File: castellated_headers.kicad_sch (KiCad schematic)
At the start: 4 parts, among them J5 Conn_01x22, J7 Conn_01x22, J8 Conn_01x22, J9 Conn_01x22

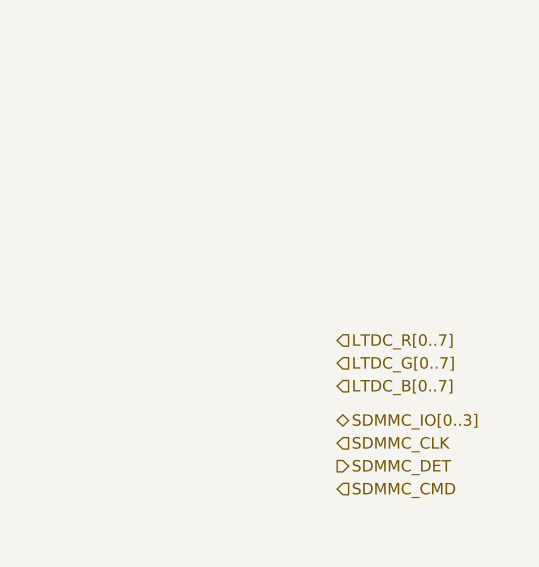
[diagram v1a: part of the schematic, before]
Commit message: Finished LTDC tracks
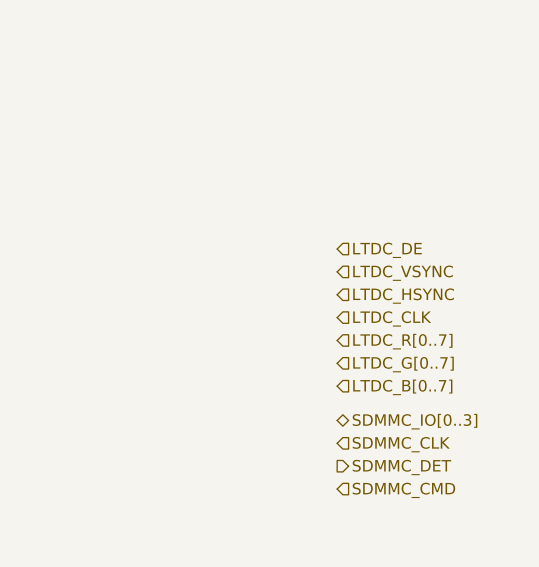
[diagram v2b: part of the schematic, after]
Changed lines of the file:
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@@
+		)
+	)
+	(hierarchical_label "LTDC_VSYNC"
+		(shape input)
+		(at 226.06 81.28 0)
+		(effects
+			(font
+				(size 1.27 1.27)
+			)
+			(justify left)
 		)
 	)
@@
 		)
 	)
+	(hierarchical_label "LTDC_HSYNC"
+		(shape input)
+		(at 226.06 83.82 0)
+		(effects
+			(font
+				(size 1.27 1.27)
+			)
+			(justify left)
+		)
+	)
 	(hierarchical_label "LTDC_R[0..7]"
 		(shape input)
@@
 		)
 	)
+	(hierarchical_label "LTDC_DE"
+		(shape input)
+		(at 226.06 78.74 0)
+		(effects
+			(font
+				(size 1.27 1.27)
+			)
+			(justify left)
+		)
+	)
 	(hierarchical_label "SWCLK"
 		(shape input)
@@
 		)
 	)
+	(hierarchical_label "LTDC_CLK"
+		(shape input)
+		(at 226.06 86.36 0)
+		(effects
+			(font
+				(size 1.27 1.27)
+			)
+			(justify left)
+		)
+	)
 	(hierarchical_label "SDMMC_IO[0..3]"
 		(shape bidirectional)
@@
 		)
 	)
+	(rule_area
+		(polyline
+			(pts
+				(xy 222.25 95.25) (xy 243.84 95.25) (xy 243.84 76.2) (xy 223.52 76.2) (xy 222.25 76.2)
+			)
+			(stroke
+				(width 0)
+				(type dash)
+			)
+			(fill
+				(type none)
+			)
+		)
+	)
+	(netclass_flag ""
+		(length 2.54)
+		(shape round)
+		(at 232.41 76.2 0)
+		(fields_autoplaced yes)
+		(effects
+			(font
+				(size 1.27 1.27)
+			)
+			(justify left bottom)
+		)
+		(property "Netclass" "LTDC"
+			(at 233.1085 73.66 0)
+			(effects
+				(font
+					(size 1.27 1.27)
+				)
+				(justify left)
+			)
+		)
+		(property "Component Class" ""
+			(at -39.37 0 0)
+			(effects
+				(font
+					(size 1.27 1.27)
+					(italic yes)
+				)
+			)
+		)
+	)

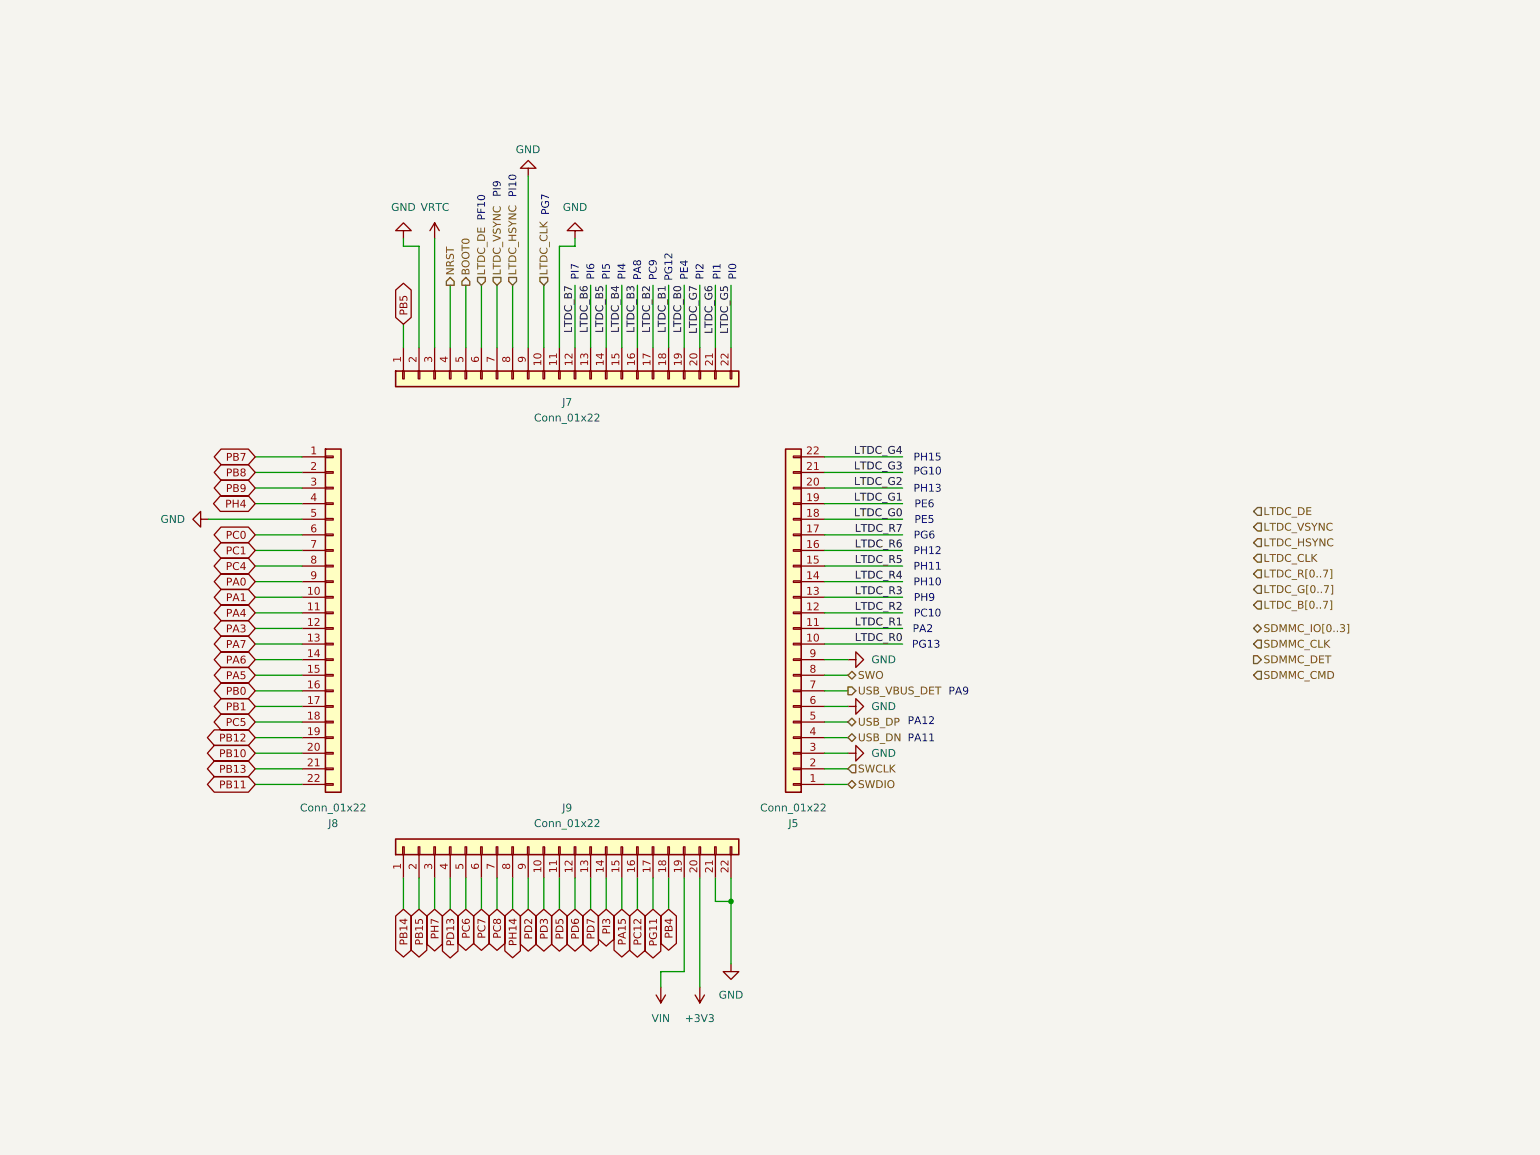
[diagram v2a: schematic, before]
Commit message: SDRAM finished, changed castellated to 23pin each side, few pins unconnected
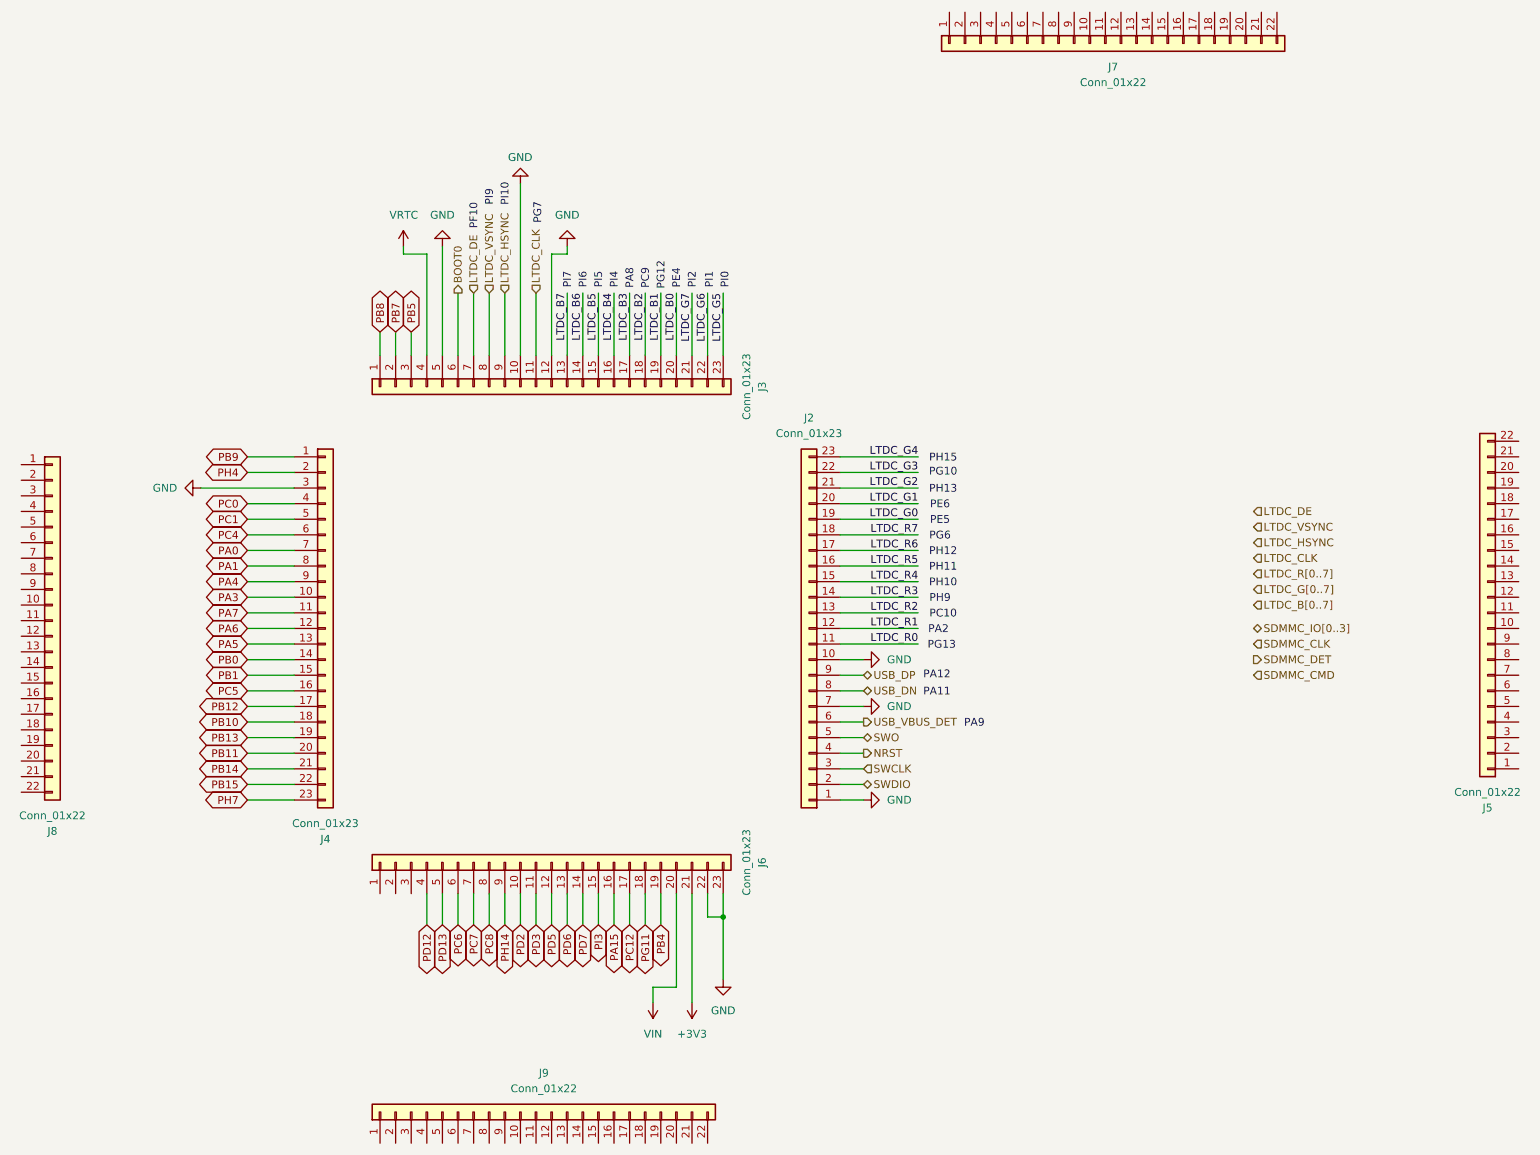
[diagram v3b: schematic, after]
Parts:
- added J2, J3, J4, J6: Conn_01x23, castellated_holes_header:castellated_01x23_P1.2mm, symbol Connector_Generic:Conn_01x23
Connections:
- net +3V3: now also J6.21 (Pin_21); no longer J9.20 (Pin_20)
- net BOOT0: now also J3.6 (Pin_6); no longer J7.5 (Pin_5)
- net GND: now also J2.1 (Pin_1), J2.10 (Pin_10), J2.7 (Pin_7), J3.10 (Pin_10), J3.12 (Pin_12), J3.5 (Pin_5), J4.3 (Pin_3), J6.22 (Pin_22), J6.23 (Pin_23); no longer J5.3 (Pin_3), J5.6 (Pin_6), J5.9 (Pin_9), J7.11 (Pin_11), J7.2 (Pin_2), J7.9 (Pin_9), J8.5 (Pin_5), J9.21 (Pin_21), J9.22 (Pin_22)
- net LTDC_B0: now also J3.20 (Pin_20); no longer J7.19 (Pin_19)
- net LTDC_B1: now also J3.19 (Pin_19); no longer J7.18 (Pin_18)
- net LTDC_B2: now also J3.18 (Pin_18); no longer J7.17 (Pin_17)
- net LTDC_B3: now also J3.17 (Pin_17); no longer J7.16 (Pin_16)
- net LTDC_B4: now also J3.16 (Pin_16); no longer J7.15 (Pin_15)
- net LTDC_B5: now also J3.15 (Pin_15); no longer J7.14 (Pin_14)
- net LTDC_B6: now also J3.14 (Pin_14); no longer J7.13 (Pin_13)
- net LTDC_B7: now also J3.13 (Pin_13); no longer J7.12 (Pin_12)
- net LTDC_CLK: now also J3.11 (Pin_11); no longer J7.10 (Pin_10)
- net LTDC_DE: now also J3.7 (Pin_7); no longer J7.6 (Pin_6)
- net LTDC_G0: now also J2.19 (Pin_19); no longer J5.18 (Pin_18)
- net LTDC_G1: now also J2.20 (Pin_20); no longer J5.19 (Pin_19)
- net LTDC_G2: now also J2.21 (Pin_21); no longer J5.20 (Pin_20)
- net LTDC_G3: now also J2.22 (Pin_22); no longer J5.21 (Pin_21)
- net LTDC_G4: now also J2.23 (Pin_23); no longer J5.22 (Pin_22)
- net LTDC_G5: now also J3.23 (Pin_23); no longer J7.22 (Pin_22)
- net LTDC_G6: now also J3.22 (Pin_22); no longer J7.21 (Pin_21)
- net LTDC_G7: now also J3.21 (Pin_21); no longer J7.20 (Pin_20)
- net LTDC_HSYNC: now also J3.9 (Pin_9); no longer J7.8 (Pin_8)
- net LTDC_R0: now also J2.11 (Pin_11); no longer J5.10 (Pin_10)
- net LTDC_R1: now also J2.12 (Pin_12); no longer J5.11 (Pin_11)
- net LTDC_R2: now also J2.13 (Pin_13); no longer J5.12 (Pin_12)
- net LTDC_R3: now also J2.14 (Pin_14); no longer J5.13 (Pin_13)
- net LTDC_R4: now also J2.15 (Pin_15); no longer J5.14 (Pin_14)
- net LTDC_R5: now also J2.16 (Pin_16); no longer J5.15 (Pin_15)
- net LTDC_R6: now also J2.17 (Pin_17); no longer J5.16 (Pin_16)
- net LTDC_R7: now also J2.18 (Pin_18); no longer J5.17 (Pin_17)
- net LTDC_VSYNC: now also J3.8 (Pin_8); no longer J7.7 (Pin_7)
- net NRST: now also J2.4 (Pin_4); no longer J7.4 (Pin_4)
- net PA0: now also J4.7 (Pin_7); no longer J8.9 (Pin_9)
- net PA1: now also J4.8 (Pin_8); no longer J8.10 (Pin_10)
- net PA15: now also J6.16 (Pin_16); no longer J9.15 (Pin_15)
- net PA3: now also J4.10 (Pin_10); no longer J8.12 (Pin_12)
- net PA4: now also J4.9 (Pin_9); no longer J8.11 (Pin_11)
- net PA5: now also J4.13 (Pin_13); no longer J8.15 (Pin_15)
- net PA6: now also J4.12 (Pin_12); no longer J8.14 (Pin_14)
- net PA7: now also J4.11 (Pin_11); no longer J8.13 (Pin_13)
- net PB0: now also J4.14 (Pin_14); no longer J8.16 (Pin_16)
- net PB1: now also J4.15 (Pin_15); no longer J8.17 (Pin_17)
- net PB10: now also J4.18 (Pin_18); no longer J8.20 (Pin_20)
- net PB11: now also J4.20 (Pin_20); no longer J8.22 (Pin_22)
- net PB12: now also J4.17 (Pin_17); no longer J8.19 (Pin_19)
- net PB13: now also J4.19 (Pin_19); no longer J8.21 (Pin_21)
- net PB14: now also J4.21 (Pin_21); no longer J9.1 (Pin_1)
- net PB15: now also J4.22 (Pin_22); no longer J9.2 (Pin_2)
- net PB4: now also J6.19 (Pin_19); no longer J9.18 (Pin_18)
- net PB5: now also J3.3 (Pin_3); no longer J7.1 (Pin_1)
- net PB7: now also J3.2 (Pin_2); no longer J8.1 (Pin_1)
- net PB8: now also J3.1 (Pin_1); no longer J8.2 (Pin_2)
- net PB9: now also J4.1 (Pin_1); no longer J8.3 (Pin_3)
- net PC0: now also J4.4 (Pin_4); no longer J8.6 (Pin_6)
- net PC1: now also J4.5 (Pin_5); no longer J8.7 (Pin_7)
- net PC12: now also J6.17 (Pin_17); no longer J9.16 (Pin_16)
- net PC4: now also J4.6 (Pin_6); no longer J8.8 (Pin_8)
- net PC5: now also J4.16 (Pin_16); no longer J8.18 (Pin_18)
- net PC6: now also J6.6 (Pin_6); no longer J9.5 (Pin_5)
- net PC7: now also J6.7 (Pin_7); no longer J9.6 (Pin_6)
- net PC8: now also J6.8 (Pin_8); no longer J9.7 (Pin_7)
- net PD13: now also J6.5 (Pin_5); no longer J9.4 (Pin_4)
- net PD2: now also J6.10 (Pin_10); no longer J9.9 (Pin_9)
- net PD3: now also J6.11 (Pin_11); no longer J9.10 (Pin_10)
- net PD5: now also J6.12 (Pin_12); no longer J9.11 (Pin_11)
- net PD6: now also J6.13 (Pin_13); no longer J9.12 (Pin_12)
- net PD7: now also J6.14 (Pin_14); no longer J9.13 (Pin_13)
- net PG11: now also J6.18 (Pin_18); no longer J9.17 (Pin_17)
- net PH14: now also J6.9 (Pin_9); no longer J9.8 (Pin_8)
- net PH4: now also J4.2 (Pin_2); no longer J8.4 (Pin_4)
- net PH7: now also J4.23 (Pin_23); no longer J9.3 (Pin_3)
- net PI3: now also J6.15 (Pin_15); no longer J9.14 (Pin_14)
- net SWCLK: now also J2.3 (Pin_3); no longer J5.2 (Pin_2)
- net SWDIO: now also J2.2 (Pin_2); no longer J5.1 (Pin_1)
- net SWO: now also J2.5 (Pin_5); no longer J5.8 (Pin_8)
- net USB_DN: now also J2.8 (Pin_8); no longer J5.4 (Pin_4)
- net USB_DP: now also J2.9 (Pin_9); no longer J5.5 (Pin_5)
- net USB_VBUS_DET: now also J2.6 (Pin_6); no longer J5.7 (Pin_7)
- net VIN: now also J6.20 (Pin_20); no longer J9.19 (Pin_19)
- net VRTC: now also J3.4 (Pin_4); no longer J7.3 (Pin_3)
- new net PD12: J6.4 (Pin_4)
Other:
- moved on the sheet: J5, J7, J8, J9
